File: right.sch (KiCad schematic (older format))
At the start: 88 parts, among them J10 UTC16-G, J18 Conn_01x01, J19 Conn_01x01, J20 Conn_01x01, J21 Conn_01x01, J22 Conn_01x01, J23 Conn_01x01, J24 Conn_01x01, J26 Buzzer_piezo, J4 reset, J5 Buzzer, J6 ISP, J8 Conn_01x01, P6 WS2812, P8 SJ-43514-SMT, SW25 Socket, SW26 Socket, SW27 Socket, SW28 Socket, SW29 Socket, SW30 Socket, SW31 Socket, SW32 Socket, SW33 Socket, SW34 Socket, SW35 Socket, SW36 Socket, SW37 Socket, SW38 Socket, SW39 Socket, SW40 Socket, SW41 Socket, SW42 Socket, SW43 Socket, SW44 Socket, SW45 Socket, SW46 Socket, SW47 Socket, SW48 Socket, SW50 FSMSM, U2 ATMega32U4, Y2 16MHz

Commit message: saved schematics
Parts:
- gave numbers to parts that had none: 1
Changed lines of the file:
@@
 Ring2
 $Comp
-L Device:R_Small R?
+L Device:R_Small R26
 U 1 1 5F84799C
 P 5425 2850
-F 0 "R?" H 5450 2875 50  0000 L CNN
+F 0 "R26" H 5450 2875 50  0000 L CNN
 F 1 "100k" H 5450 2800 50  0000 L CNN
 F 2 "Resistor_SMD:R_0603_1608Metric" H 5425 2850 50  0001 C CNN
@@
 P 5650 2900
 AR Path="/5A0DE9BD/5F848EE3" Ref="#PWR?"  Part="1"
-AR Path="/5A0DF911/5F848EE3" Ref="#PWR?"  Part="1"
-F 0 "#PWR?" H 5650 2650 50  0001 C CNN
+AR Path="/5A0DF911/5F848EE3" Ref="#PWR0125"  Part="1"
+F 0 "#PWR0125" H 5650 2650 50  0001 C CNN
 F 1 "GND" H 5650 2750 50  0000 C CNN
 F 2 "" H 5650 2900 50  0000 C CNN

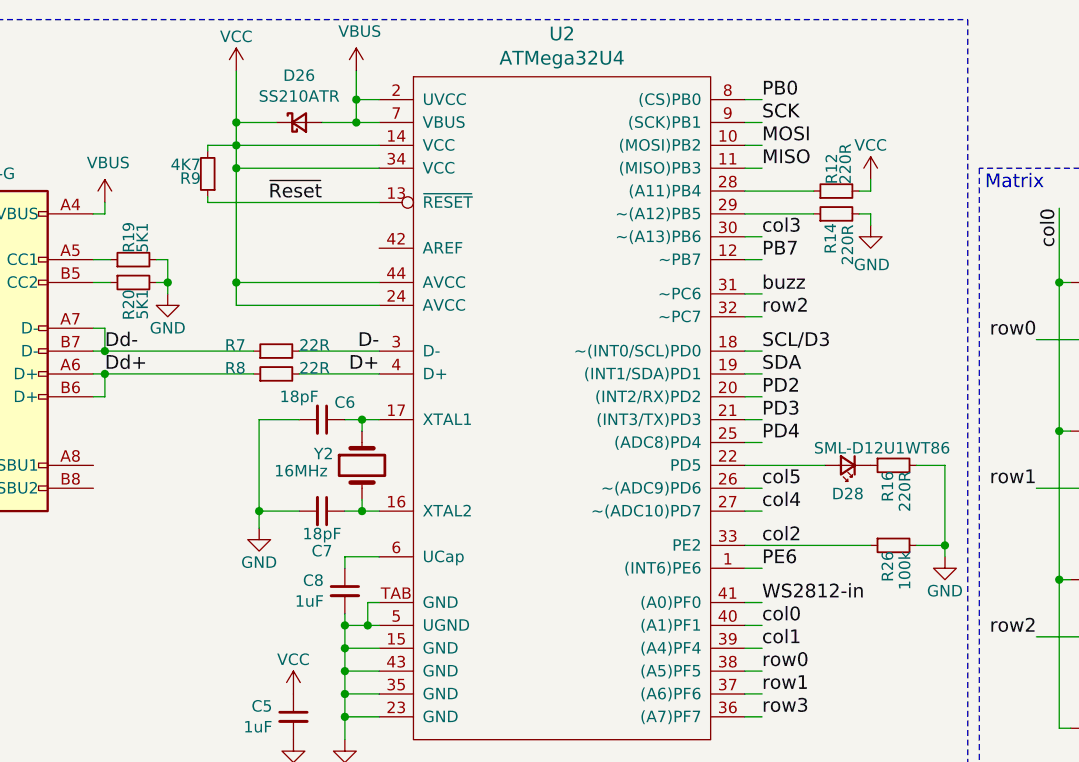
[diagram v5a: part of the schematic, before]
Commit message: Updated I2C pull-up values
Updated the values to ensure the effect of the newly added series resistors don't cause the low level to exceed chip specifications for i2c potentially leading to communication issues if using i2c
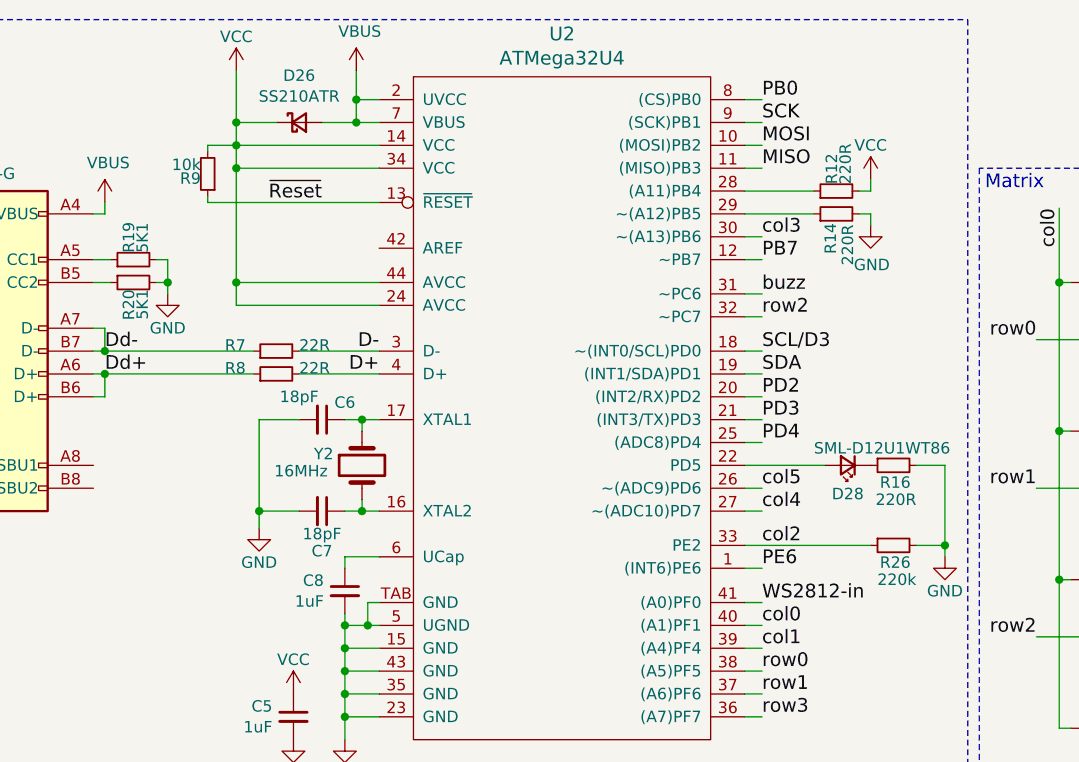
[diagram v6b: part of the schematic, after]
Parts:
- R26: value 100k -> 220k
- R9: value 4K7 -> 10k
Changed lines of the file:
@@
 P 2425 1225
 F 0 "R9" H 2455 1245 50  0000 L CNN
-F 1 "4K7" H 2455 1185 50  0000 L CNN
+F 1 "10k" H 2455 1185 50  0000 L CNN
 F 2 "Resistor_SMD:R_0603_1608Metric" H 2425 1225 50  0001 C CNN
 F 3 "" H 2425 1225 50  0000 C CNN
@@
 U 1 1 5B5FD571
 P 5425 2500
-F 0 "R16" H 5450 2525 50  0000 L CNN
-F 1 "220R" H 5450 2450 50  0000 L CNN
+F 0 "R16" V 5500 2425 50  0000 L CNN
+F 1 "220R" V 5575 2400 50  0000 L CNN
 F 2 "Resistor_SMD:R_0603_1608Metric" H 5425 2500 50  0001 C CNN
 F 3 "" H 5425 2500 50  0000 C CNN
@@
 U 1 1 5F84799C
 P 5425 2850
-F 0 "R26" H 5450 2875 50  0000 L CNN
-F 1 "100k" H 5450 2800 50  0000 L CNN
+F 0 "R26" V 5500 2775 50  0000 L CNN
+F 1 "220k" V 5575 2750 50  0000 L CNN
 F 2 "Resistor_SMD:R_0603_1608Metric" H 5425 2850 50  0001 C CNN
 F 3 "" H 5425 2850 50  0000 C CNN
